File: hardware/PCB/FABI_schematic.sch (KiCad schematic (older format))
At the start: 26 parts, among them J1 PJ307, J10 Conn_01x03_Male, J2 PJ307, J3 PJ307, J4 PJ307, J5 PJ307, J6 PJ307, J7 PJ307, J8 PJ307, J9 Conn_02x05_Odd_Even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

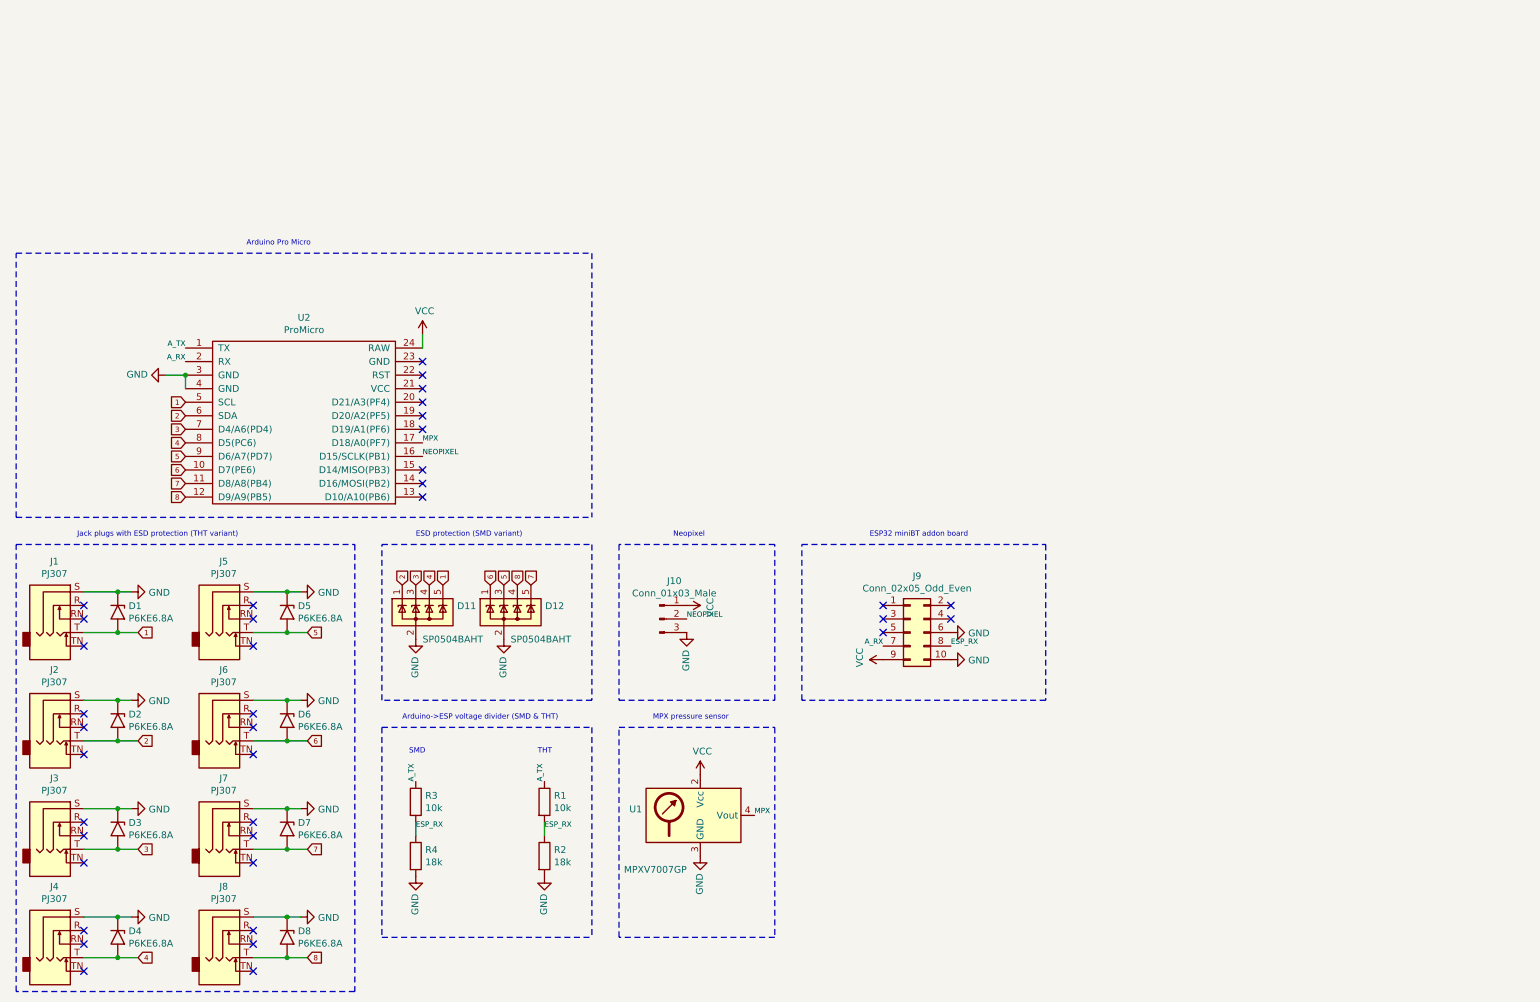
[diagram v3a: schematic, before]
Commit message: redesign of PCB, Jackplugs updatet, Buzzer added, TVS repositioned
Signed-off-by: fussthalerandreas <fussthaler.andreas1997@gmail.com>
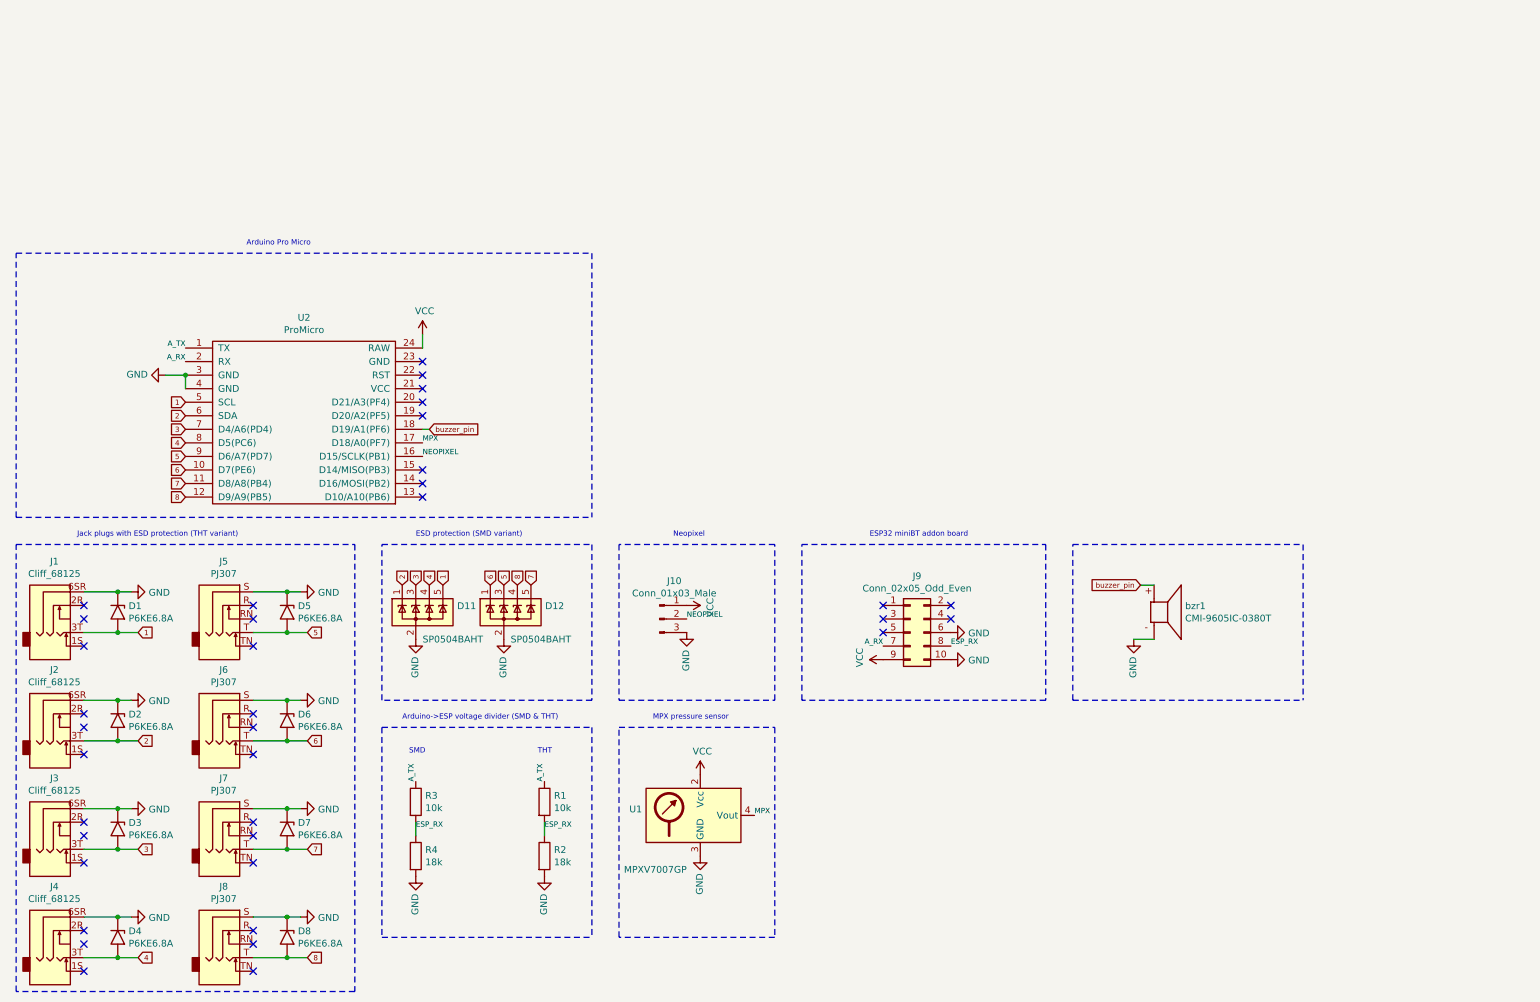
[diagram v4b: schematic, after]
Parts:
- removed J1, J2, J3, J4: PJ307, PJ307:PJ-307, symbol Connector:AudioJack3_SwitchTR
- added J1, J2, J3, J4: Cliff_68125, CLIFF_FC68125:CLIFF_FC68125, symbol Connector:Cliff_68125
- added bzr1: CMI-9605IC-0380T, CMI-9605IC-0380T:CUI_CMI-9605IC-0380T, symbol CMI-9605IC-0380T:CMI-9605IC-0380T
- D1, D2, D3, D5, D6, D7, D8: footprint Diode_THT:D_DO-201AE_P5.08mm_Vertical_KathodeUp -> Diode_THT:D_DO-201AE_P12.70mm_Horizontal
- D4: footprint Diode_THT:D_DO-201AE_P5.08mm_Vertical_KathodeUp -> Diode_THT:D_DO-201AD_P12.70mm_Horizontal
- J5, J6, J7, J8: footprint PJ307:PJ-307 -> CLIFF_FC68125:CLIFF_FC68125
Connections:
- net 1: now also J1.3T
- net 2: now also J2.3T
- net 3: now also J3.3T
- net 4: now also J4.3T
- net GND: now also J1.6SR, J2.6SR, J3.6SR, J4.6SR, bzr1.N
- net buzzer_pin: now reaches U2.18 (D19/A1(PF6))
- net buzzer_pin: now also bzr1.P
- no-connect marks 38 -> 37
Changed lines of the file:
@@
 NoConn ~ 3600 3250
 NoConn ~ 3600 3350
-NoConn ~ 3600 3550
 NoConn ~ 3600 3850
 NoConn ~ 3600 3950
@@
 	0    1    -1   0
 $EndComp
-$Comp
-L Connector:AudioJack3_SwitchTR J1
-U 1 1 5F38607E
-P 900 4850
-F 0 "J1" H 882 5175 50  0000 C CNN
-F 1 "PJ307" H 882 5084 50  0000 C CNN
-F 2 "PJ307:PJ-307" H 900 4850 50  0001 C CNN
-F 3 "~" H 900 4850 50  0001 C CNN
-F 4 "2518188" H 900 4850 50  0001 C CNN "Farnell"
-F 5 "913-1021" H 900 4850 50  0001 C CNN "RS-components"
-	1    900  4850
-	1    0    0    -1
-$EndComp
-NoConn ~ 1100 5150
 NoConn ~ 1100 4950
 NoConn ~ 1100 4850
@@
 Text GLabel 1500 5050 2    39   Input ~ 0
 1
-$Comp
-L Connector:AudioJack3_SwitchTR J2
-U 1 1 5F399A19
-P 900 5650
-F 0 "J2" H 882 5975 50  0000 C CNN
-F 1 "PJ307" H 882 5884 50  0000 C CNN
-F 2 "PJ307:PJ-307" H 900 5650 50  0001 C CNN
-F 3 "~" H 900 5650 50  0001 C CNN
-	1    900  5650
-	1    0    0    -1
-$EndComp
 NoConn ~ 1100 5950
 NoConn ~ 1100 5750
@@
 NoConn ~ 1100 6550
 NoConn ~ 1100 6750
-$Comp
-L Connector:AudioJack3_SwitchTR J3
-U 1 1 5F39BF0B
-P 900 6450
-F 0 "J3" H 882 6775 50  0000 C CNN
-F 1 "PJ307" H 882 6684 50  0000 C CNN
-F 2 "PJ307:PJ-307" H 900 6450 50  0001 C CNN
-F 3 "~" H 900 6450 50  0001 C CNN
-	1    900  6450
-	1    0    0    -1
-$EndComp
-$Comp
-L Connector:AudioJack3_SwitchTR J4
-U 1 1 5F3A80ED
-P 900 7250
-F 0 "J4" H 882 7575 50  0000 C CNN
-F 1 "PJ307" H 882 7484 50  0000 C CNN
-F 2 "PJ307:PJ-307" H 900 7250 50  0001 C CNN
-F 3 "~" H 900 7250 50  0001 C CNN
-	1    900  7250
-	1    0    0    -1
-$EndComp
 NoConn ~ 1100 7550
 NoConn ~ 1100 7350
@@
 F 0 "J5" H 2132 5175 50  0000 C CNN
 F 1 "PJ307" H 2132 5084 50  0000 C CNN
-F 2 "PJ307:PJ-307" H 2150 4850 50  0001 C CNN
+F 2 "CLIFF_FC68125:CLIFF_FC68125" H 2150 4850 50  0001 C CNN
 F 3 "~" H 2150 4850 50  0001 C CNN
 	1    2150 4850
@@
 F 0 "J6" H 2132 5975 50  0000 C CNN
 F 1 "PJ307" H 2132 5884 50  0000 C CNN
-F 2 "PJ307:PJ-307" H 2150 5650 50  0001 C CNN
+F 2 "CLIFF_FC68125:CLIFF_FC68125" H 2150 5650 50  0001 C CNN
 F 3 "~" H 2150 5650 50  0001 C CNN
 	1    2150 5650
@@
 F 0 "J7" H 2132 6775 50  0000 C CNN
 F 1 "PJ307" H 2132 6684 50  0000 C CNN
-F 2 "PJ307:PJ-307" H 2150 6450 50  0001 C CNN
+F 2 "CLIFF_FC68125:CLIFF_FC68125" H 2150 6450 50  0001 C CNN
 F 3 "~" H 2150 6450 50  0001 C CNN
 	1    2150 6450
@@
 F 0 "J8" H 2132 7575 50  0000 C CNN
 F 1 "PJ307" H 2132 7484 50  0000 C CNN
-F 2 "PJ307:PJ-307" H 2150 7250 50  0001 C CNN
+F 2 "CLIFF_FC68125:CLIFF_FC68125" H 2150 7250 50  0001 C CNN
 F 3 "~" H 2150 7250 50  0001 C CNN
 	1    2150 7250
@@
 F 0 "D1" V 1304 4980 50  0000 L CNN
 F 1 "P6KE6.8A" V 1395 4980 50  0000 L CNN
-F 2 "Diode_THT:D_DO-201AE_P5.08mm_Vertical_KathodeUp" H 1350 4700 50  0001 C CNN
+F 2 "Diode_THT:D_DO-201AE_P12.70mm_Horizontal" H 1350 4700 50  0001 C CNN
 F 3 "https://www.vishay.com/docs/88301/15ke.pdf" H 1300 4900 50  0001 C CNN
 F 4 "1703028" V 1350 4900 50  0001 C CNN "Farnell"
@@
 F 0 "D2" V 1304 5780 50  0000 L CNN
 F 1 "P6KE6.8A" V 1395 5780 50  0000 L CNN
-F 2 "Diode_THT:D_DO-201AE_P5.08mm_Vertical_KathodeUp" H 1350 5500 50  0001 C CNN
+F 2 "Diode_THT:D_DO-201AE_P12.70mm_Horizontal" H 1350 5500 50  0001 C CNN
 F 3 "https://www.vishay.com/docs/88301/15ke.pdf" H 1300 5700 50  0001 C CNN
 	1    1350 5700
@@
 F 0 "D3" V 1304 6580 50  0000 L CNN
 F 1 "P6KE6.8A" V 1395 6580 50  0000 L CNN
-F 2 "Diode_THT:D_DO-201AE_P5.08mm_Vertical_KathodeUp" H 1350 6300 50  0001 C CNN
+F 2 "Diode_THT:D_DO-201AE_P12.70mm_Horizontal" H 1350 6300 50  0001 C CNN
 F 3 "https://www.vishay.com/docs/88301/15ke.pdf" H 1300 6500 50  0001 C CNN
 	1    1350 6500
@@
 F 0 "D4" V 1304 7380 50  0000 L CNN
 F 1 "P6KE6.8A" V 1395 7380 50  0000 L CNN
-F 2 "Diode_THT:D_DO-201AE_P5.08mm_Vertical_KathodeUp" H 1350 7100 50  0001 C CNN
+F 2 "Diode_THT:D_DO-201AD_P12.70mm_Horizontal" H 1350 7100 50  0001 C CNN
 F 3 "https://www.vishay.com/docs/88301/15ke.pdf" H 1300 7300 50  0001 C CNN
 	1    1350 7300
@@
 F 0 "D5" V 2554 4980 50  0000 L CNN
 F 1 "P6KE6.8A" V 2645 4980 50  0000 L CNN
-F 2 "Diode_THT:D_DO-201AE_P5.08mm_Vertical_KathodeUp" H 2600 4700 50  0001 C CNN
+F 2 "Diode_THT:D_DO-201AE_P12.70mm_Horizontal" H 2600 4700 50  0001 C CNN
 F 3 "https://www.vishay.com/docs/88301/15ke.pdf" H 2550 4900 50  0001 C CNN
 	1    2600 4900
@@
 F 0 "D6" V 2554 5780 50  0000 L CNN
 F 1 "P6KE6.8A" V 2645 5780 50  0000 L CNN
-F 2 "Diode_THT:D_DO-201AE_P5.08mm_Vertical_KathodeUp" H 2600 5500 50  0001 C CNN
+F 2 "Diode_THT:D_DO-201AE_P12.70mm_Horizontal" H 2600 5500 50  0001 C CNN
 F 3 "https://www.vishay.com/docs/88301/15ke.pdf" H 2550 5700 50  0001 C CNN
 	1    2600 5700
@@
 F 0 "D7" V 2554 6580 50  0000 L CNN
 F 1 "P6KE6.8A" V 2645 6580 50  0000 L CNN
-F 2 "Diode_THT:D_DO-201AE_P5.08mm_Vertical_KathodeUp" H 2600 6300 50  0001 C CNN
+F 2 "Diode_THT:D_DO-201AE_P12.70mm_Horizontal" H 2600 6300 50  0001 C CNN
 F 3 "https://www.vishay.com/docs/88301/15ke.pdf" H 2550 6500 50  0001 C CNN
 	1    2600 6500
@@
 F 0 "D8" V 2554 7380 50  0000 L CNN
 F 1 "P6KE6.8A" V 2645 7380 50  0000 L CNN
-F 2 "Diode_THT:D_DO-201AE_P5.08mm_Vertical_KathodeUp" H 2600 7100 50  0001 C CNN
+F 2 "Diode_THT:D_DO-201AE_P12.70mm_Horizontal" H 2600 7100 50  0001 C CNN
 F 3 "https://www.vishay.com/docs/88301/15ke.pdf" H 2550 7300 50  0001 C CNN
 	1    2600 7300
@@
 	600  7700 600  4400
 Wire Notes Line
-	3300 4400 4850 4400
-Wire Notes Line
-	4850 4400 4850 5550
-Wire Notes Line
 	4850 5550 3300 5550
 Wire Notes Line
@@
 Text Label 3600 3750 0    39   ~ 0
 NEOPIXEL
+Wire Notes Line
+	4850 4400 4850 5550
+Wire Notes Line
+	3300 4400 4850 4400
+Text GLabel 3650 3550 2    39   Input ~ 0
+buzzer_pin
+Text GLabel 8900 4700 0    39   Input ~ 0
+buzzer_pin
+$Comp
+L power:GND #PWR0101
+U 1 1 602224F3
+P 8850 5100
+F 0 "#PWR0101" H 8850 4850 50  0001 C CNN
+F 1 "GND" V 8855 4972 50  0000 R CNN
+F 2 "" H 8850 5100 50  0001 C CNN
+F 3 "" H 8850 5100 50  0001 C CNN
+	1    8850 5100
+	-1   0    0    -1
+$EndComp
+Wire Wire Line
+	8850 5100 9000 5100
+Wire Wire Line
+	8900 4700 9000 4700
+Wire Wire Line
+	3600 3550 3650 3550
+Wire Notes Line
+	10100 4400 10100 5550
+Wire Notes Line
+	8400 5550 8400 4400
+Wire Notes Line
+	8400 4400 10100 4400
+Wire Notes Line
+	8400 5550 10100 5550
+$Comp
+L CMI-9605IC-0380T:CMI-9605IC-0380T bzr1
+U 1 1 60230DDB
+P 9100 4900
+F 0 "bzr1" H 9229 4946 50  0000 L CNN
+F 1 "CMI-9605IC-0380T" H 9229 4855 50  0000 L CNN
+F 2 "CMI-9605IC-0380T:CUI_CMI-9605IC-0380T" H 9100 4900 50  0001 L BNN
+F 3 "" H 9100 4900 50  0001 L BNN
+F 4 "1.0" H 9100 4900 50  0001 L BNN "PARTREV"
+F 5 "5.00mm" H 9100 4900 50  0001 L BNN "MAXIMUM_PACKAGE_HEIGHT"
+F 6 "Manufacturer Recommendations" H 9100 4900 50  0001 L BNN "STANDARD"
+F 7 "CUI Inc." H 9100 4900 50  0001 L BNN "MANUFACTURER"
+	1    9100 4900
+	1    0    0    -1
+$EndComp
+$Comp
+L Connector:Cliff_68125 J2
+U 1 1 601CD635
+P 900 5650
+F 0 "J2" H 882 5975 50  0000 C CNN
+F 1 "Cliff_68125" H 882 5884 50  0000 C CNN
+F 2 "CLIFF_FC68125:CLIFF_FC68125" H 900 5650 50  0001 C CNN
+F 3 "~" H 900 5650 50  0001 C CNN
+	1    900  5650
+	1    0    0    -1
+$EndComp
+$Comp
+L Connector:Cliff_68125 J1
+U 1 1 601CBF3E
+P 900 4850
+F 0 "J1" H 882 5175 50  0000 C CNN
+F 1 "Cliff_68125" H 882 5084 50  0000 C CNN
+F 2 "CLIFF_FC68125:CLIFF_FC68125" H 900 4850 50  0001 C CNN
+F 3 "~" H 900 4850 50  0001 C CNN
+	1    900  4850
+	1    0    0    -1
+$EndComp
+NoConn ~ 1100 5150
+$Comp
+L Connector:Cliff_68125 J3
+U 1 1 601FBFE8
+P 900 6450
+F 0 "J3" H 882 6775 50  0000 C CNN
+F 1 "Cliff_68125" H 882 6684 50  0000 C CNN
+F 2 "CLIFF_FC68125:CLIFF_FC68125" H 900 6450 50  0001 C CNN
+F 3 "~" H 900 6450 50  0001 C CNN
+	1    900  6450
+	1    0    0    -1
+$EndComp
+$Comp
+L Connector:Cliff_68125 J4
+U 1 1 601FCE09
+P 900 7250
+F 0 "J4" H 882 7575 50  0000 C CNN
+F 1 "Cliff_68125" H 882 7484 50  0000 C CNN
+F 2 "CLIFF_FC68125:CLIFF_FC68125" H 900 7250 50  0001 C CNN
+F 3 "~" H 900 7250 50  0001 C CNN
+	1    900  7250
+	1    0    0    -1
+$EndComp
 $EndSCHEMATC

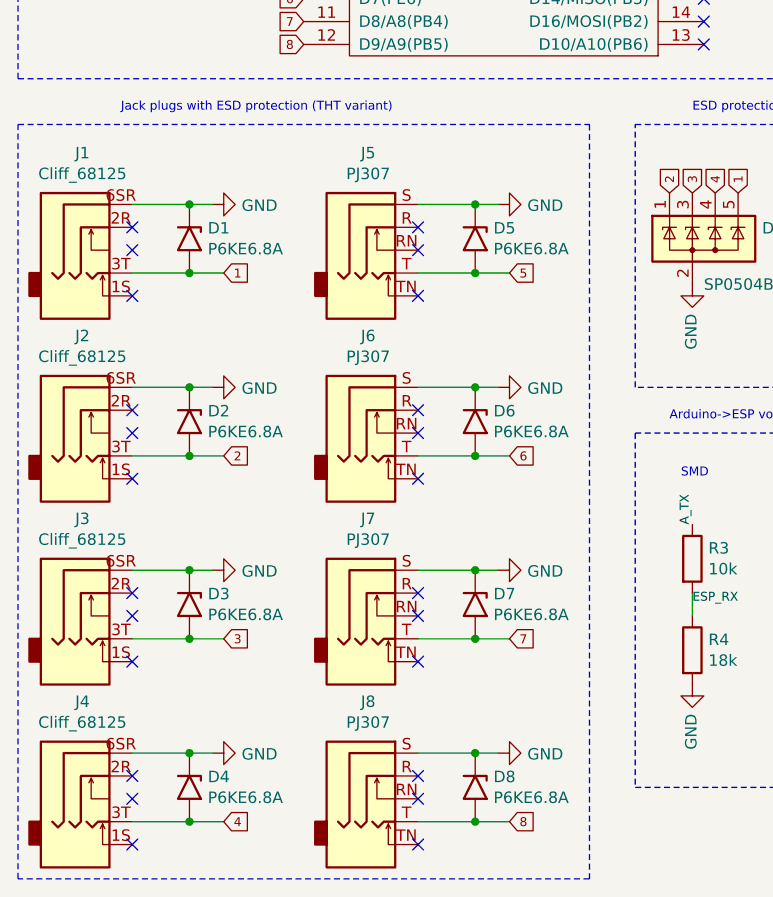
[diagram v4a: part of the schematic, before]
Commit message: new schematics PDF
Signed-off-by: fussthalerandreas <fussthaler.andreas1997@gmail.com>
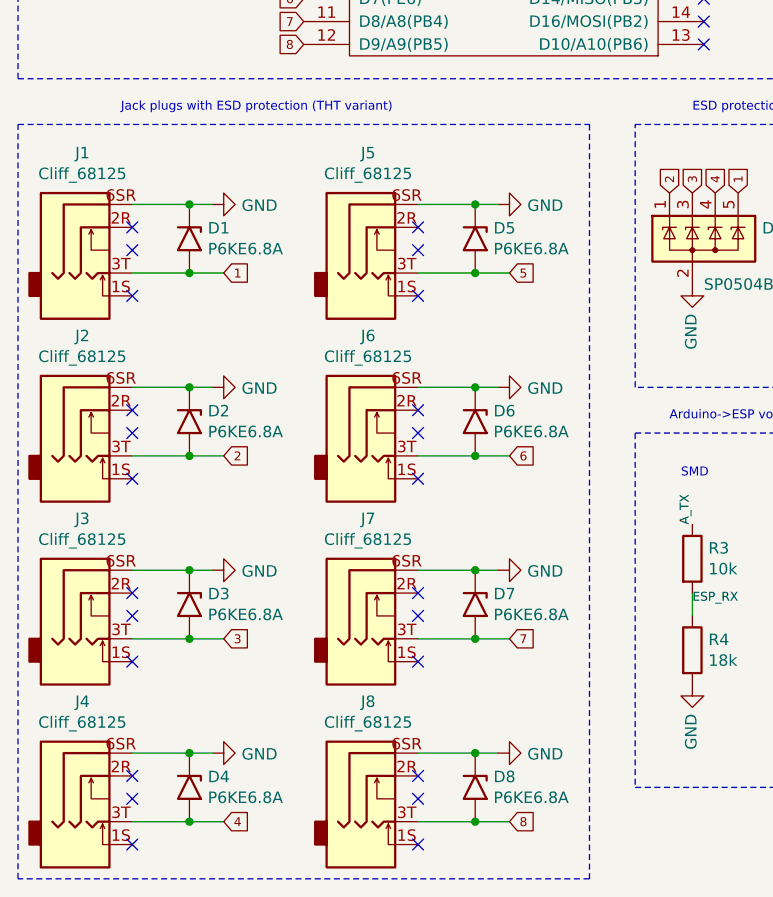
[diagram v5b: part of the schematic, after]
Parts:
- removed J5, J6, J7, J8: PJ307, CLIFF_FC68125:CLIFF_FC68125, symbol Connector:AudioJack3_SwitchTR
- added J5, J6, J7, J8: Cliff_68125, CLIFF_FC68125:CLIFF_FC68125, symbol Connector:Cliff_68125
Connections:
- net 5: now also J5.3T
- net 6: now also J6.3T
- net 7: now also J7.3T
- net 8: now also J8.3T
- net GND: now also J5.6SR, J6.6SR, J7.6SR, J8.6SR
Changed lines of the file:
@@
 Text GLabel 1500 7450 2    39   Input ~ 0
 4
-$Comp
-L Connector:AudioJack3_SwitchTR J5
-U 1 1 5F3B6393
-P 2150 4850
-F 0 "J5" H 2132 5175 50  0000 C CNN
-F 1 "PJ307" H 2132 5084 50  0000 C CNN
-F 2 "CLIFF_FC68125:CLIFF_FC68125" H 2150 4850 50  0001 C CNN
-F 3 "~" H 2150 4850 50  0001 C CNN
-	1    2150 4850
-	1    0    0    -1
-$EndComp
 NoConn ~ 2350 5150
 NoConn ~ 2350 4950
@@
 Text GLabel 2750 5050 2    39   Input ~ 0
 5
-$Comp
-L Connector:AudioJack3_SwitchTR J6
-U 1 1 5F3B63AF
-P 2150 5650
-F 0 "J6" H 2132 5975 50  0000 C CNN
-F 1 "PJ307" H 2132 5884 50  0000 C CNN
-F 2 "CLIFF_FC68125:CLIFF_FC68125" H 2150 5650 50  0001 C CNN
-F 3 "~" H 2150 5650 50  0001 C CNN
-	1    2150 5650
-	1    0    0    -1
-$EndComp
 NoConn ~ 2350 5950
 NoConn ~ 2350 5750
@@
 NoConn ~ 2350 6550
 NoConn ~ 2350 6750
-$Comp
-L Connector:AudioJack3_SwitchTR J7
-U 1 1 5F3B63E1
-P 2150 6450
-F 0 "J7" H 2132 6775 50  0000 C CNN
-F 1 "PJ307" H 2132 6684 50  0000 C CNN
-F 2 "CLIFF_FC68125:CLIFF_FC68125" H 2150 6450 50  0001 C CNN
-F 3 "~" H 2150 6450 50  0001 C CNN
-	1    2150 6450
-	1    0    0    -1
-$EndComp
-$Comp
-L Connector:AudioJack3_SwitchTR J8
-U 1 1 5F3B63E7
-P 2150 7250
-F 0 "J8" H 2132 7575 50  0000 C CNN
-F 1 "PJ307" H 2132 7484 50  0000 C CNN
-F 2 "CLIFF_FC68125:CLIFF_FC68125" H 2150 7250 50  0001 C CNN
-F 3 "~" H 2150 7250 50  0001 C CNN
-	1    2150 7250
-	1    0    0    -1
-$EndComp
 NoConn ~ 2350 7550
 NoConn ~ 2350 7350
@@
 	2350 6650 2600 6650
 Wire Wire Line
-	2350 5550 2600 5550
-Wire Wire Line
-	2350 5850 2600 5850
-Wire Wire Line
 	2350 4750 2600 4750
 Wire Wire Line
@@
 	1    0    0    -1
 $EndComp
+$Comp
+L Connector:Cliff_68125 J5
+U 1 1 60206E96
+P 2150 4850
+F 0 "J5" H 2132 5175 50  0000 C CNN
+F 1 "Cliff_68125" H 2132 5084 50  0000 C CNN
+F 2 "CLIFF_FC68125:CLIFF_FC68125" H 2150 4850 50  0001 C CNN
+F 3 "~" H 2150 4850 50  0001 C CNN
+	1    2150 4850
+	1    0    0    -1
+$EndComp
+$Comp
+L Connector:Cliff_68125 J6
+U 1 1 60207C3C
+P 2150 5650
+F 0 "J6" H 2132 5975 50  0000 C CNN
+F 1 "Cliff_68125" H 2132 5884 50  0000 C CNN
+F 2 "CLIFF_FC68125:CLIFF_FC68125" H 2150 5650 50  0001 C CNN
+F 3 "~" H 2150 5650 50  0001 C CNN
+	1    2150 5650
+	1    0    0    -1
+$EndComp
+$Comp
+L Connector:Cliff_68125 J7
+U 1 1 6020893A
+P 2150 6450
+F 0 "J7" H 2132 6775 50  0000 C CNN
+F 1 "Cliff_68125" H 2132 6684 50  0000 C CNN
+F 2 "CLIFF_FC68125:CLIFF_FC68125" H 2150 6450 50  0001 C CNN
+F 3 "~" H 2150 6450 50  0001 C CNN
+	1    2150 6450
+	1    0    0    -1
+$EndComp
+$Comp
+L Connector:Cliff_68125 J8
+U 1 1 6020964B
+P 2150 7250
+F 0 "J8" H 2132 7575 50  0000 C CNN
+F 1 "Cliff_68125" H 2132 7484 50  0000 C CNN
+F 2 "CLIFF_FC68125:CLIFF_FC68125" H 2150 7250 50  0001 C CNN
+F 3 "~" H 2150 7250 50  0001 C CNN
+	1    2150 7250
+	1    0    0    -1
+$EndComp
+Wire Wire Line
+	2350 5550 2600 5550
+Wire Wire Line
+	2350 5850 2600 5850
 $EndSCHEMATC
